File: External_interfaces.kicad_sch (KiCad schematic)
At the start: 31 parts, among them J10 Conn_01x06_Pin, J15 Conn_01x02_Pin, J17 Conn_01x04_Pin, J7 Conn_01x02_Pin, J8 Conn_01x06_Pin, J9 Conn_01x02_Pin, Q1 AO3400A, Q2 AO3400A

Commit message: feat:убрал часть с батарейным питанием, убрал лишние элементы со старого проекта
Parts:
- removed C28, C45, C46, C47, C52: 0.1u, Capacitor_SMD:C_0805_2012Metric_Pad1.18x1.45mm_HandSolder, symbol Device:C_Small
- removed D4, D5: SMAJ30CA, Diode_SMD:D_SMA, symbol Diode:SMAJ30CA
- removed J10, J8: Conn_01x06_Pin, Connector_Hirose:Hirose_DF13-06P-1.25DSA_1x06_P1.25mm_Vertical, symbol Connector:Conn_01x06_Pin
- removed J15, J7: Conn_01x02_Pin, Connector_PinHeader_2.54mm:PinHeader_1x02_P2.54mm_Vertical, symbol Connector:Conn_01x02_Pin
- removed J17: Conn_01x04_Pin, Connector_PinSocket_2.54mm:PinSocket_1x04_P2.54mm_Vertical, symbol Connector:Conn_01x04_Pin
- removed J9: Conn_01x02_Pin, Connector_Hirose:Hirose_DF13-02P-1.25DSA_1x02_P1.25mm_Vertical, symbol Connector:Conn_01x02_Pin
- removed Q1, Q2: AO3400A, Package_TO_SOT_SMD:SOT-23, symbol Transistor_FET:AO3400A
- removed R23, R24, R27, R28, R31, R32: 0, Resistor_SMD:R_0805_2012Metric_Pad1.20x1.40mm_HandSolder, symbol Device:R
- removed R25, R29: 100, Resistor_SMD:R_0805_2012Metric_Pad1.20x1.40mm_HandSolder, symbol Device:R
- removed R26, R30: 10k, Resistor_SMD:R_0805_2012Metric_Pad1.20x1.40mm_HandSolder, symbol Device:R
- removed R7, R8: 3k, Resistor_SMD:R_0805_2012Metric_Pad1.20x1.40mm_HandSolder, symbol Device:R
- removed VD10, VD15, VD2, VD3: GSOT03C-E3-08, Package_TO_SOT_SMD:SOT-23, symbol TWS:GSOT03C-E3-08
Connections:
- no-connect marks 4 -> 0

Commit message: feaat: добавлены светодиоды, кнопки и недостающие элементы защиты питания
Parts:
- added C60, C61, C62, C63, C64, C65, C66, C67, C68, C69, C70, C71: 0.1u, Capacitor_SMD:C_0805_2012Metric_Pad1.18x1.45mm_HandSolder, symbol Device:C_Small
- added R28, R33, R34, R35, R37, R38, R39, R40, R41, R42, R43, R44: 100, Resistor_SMD:R_0805_2012Metric_Pad1.20x1.40mm_HandSolder, symbol Device:R
- added SW1, SW10, SW11, SW12, SW2, SW3, SW4, SW5, SW6, SW7, SW8, SW9: SW_Push, Button_Switch_THT:SW_PUSH_6mm, symbol Switch:SW_Push
- added VD10, VD4, VD5, VD7, VD8, VD9: GSOT03C-E3-08, Package_TO_SOT_SMD:SOT-23_Handsoldering, symbol TVS_1:GSOT03C-E3-08
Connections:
- new net: C71.2, R44.1
- new net: R44.2, SW12.1, VD10.2 (K2)
- new net: R33.2, SW2.1, VD4.2 (K2)
- new net: R37.2, SW5.1, VD7.1 (K1)
- new net: R39.2, SW7.1, VD8.1 (K1)
- new net: R40.2, SW8.1, VD8.2 (K2)
- new net: C70.2, R43.1
- new net: C65.2, R42.1
- new net: R42.2, SW10.1, VD9.2 (K2)
- new net: R41.2, SW9.1, VD9.1 (K1)
- new net: R34.2, SW3.1, VD5.1 (K1)
- new net: R35.2, SW4.1, VD5.2 (K2)
- new net: R43.2, SW11.1, VD10.1 (K1)
- new net: C62.2, R37.1
- new net: C64.2, R41.1
- new net: R28.2, SW1.1, VD4.1 (K1)
- new net: C69.2, R40.1
- new net: C63.2, R38.1
- new net: R38.2, SW6.1, VD7.2 (K2)
- new net: C68.2, R39.1
- new net DI1: C60.2, R28.1
- new net DI2: C61.2, R33.1
- new net DI3: C67.2, R34.1
- new net DI4: C66.2, R35.1
- new net GND: C60.1, C61.1, C62.1, C63.1, C64.1, C65.1, C66.1, C67.1, C68.1, C69.1, C70.1, C71.1, SW1.2, SW10.2, SW11.2, SW12.2, SW2.2, SW3.2, SW4.2, SW5.2, SW6.2, SW7.2, SW8.2, SW9.2, VD10.3 (A), VD4.3 (A), VD5.3 (A), VD7.3 (A), VD8.3 (A), VD9.3 (A)

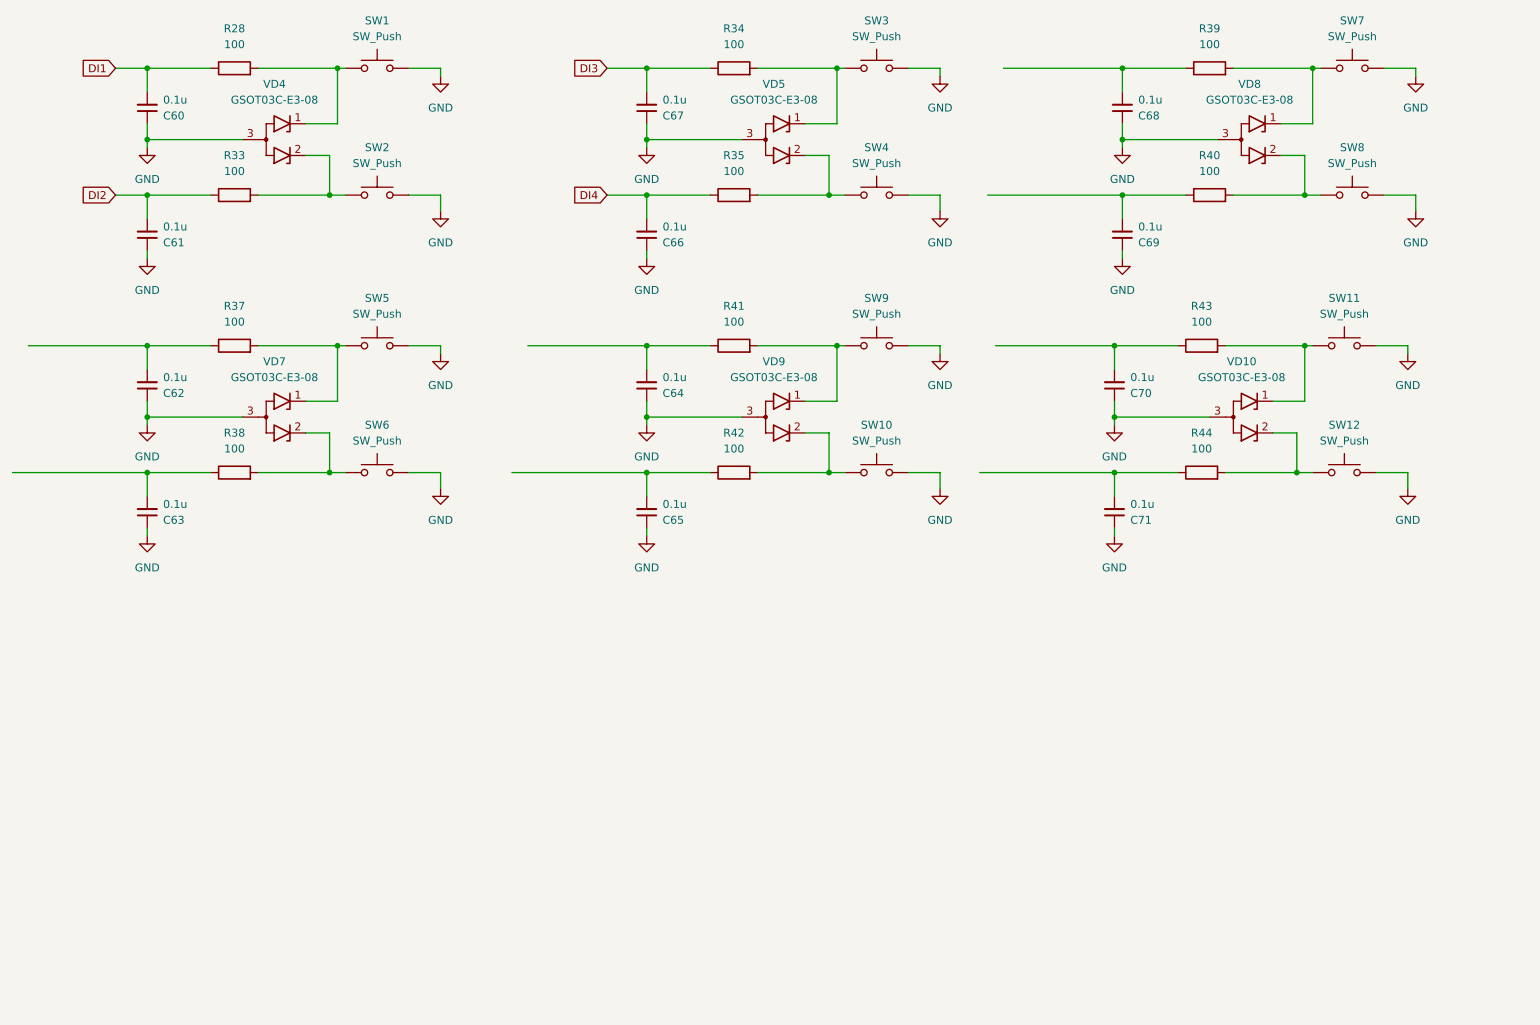
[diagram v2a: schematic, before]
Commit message: feat: добавлены глобальные линии связи, удалены линии связи со старого проекта
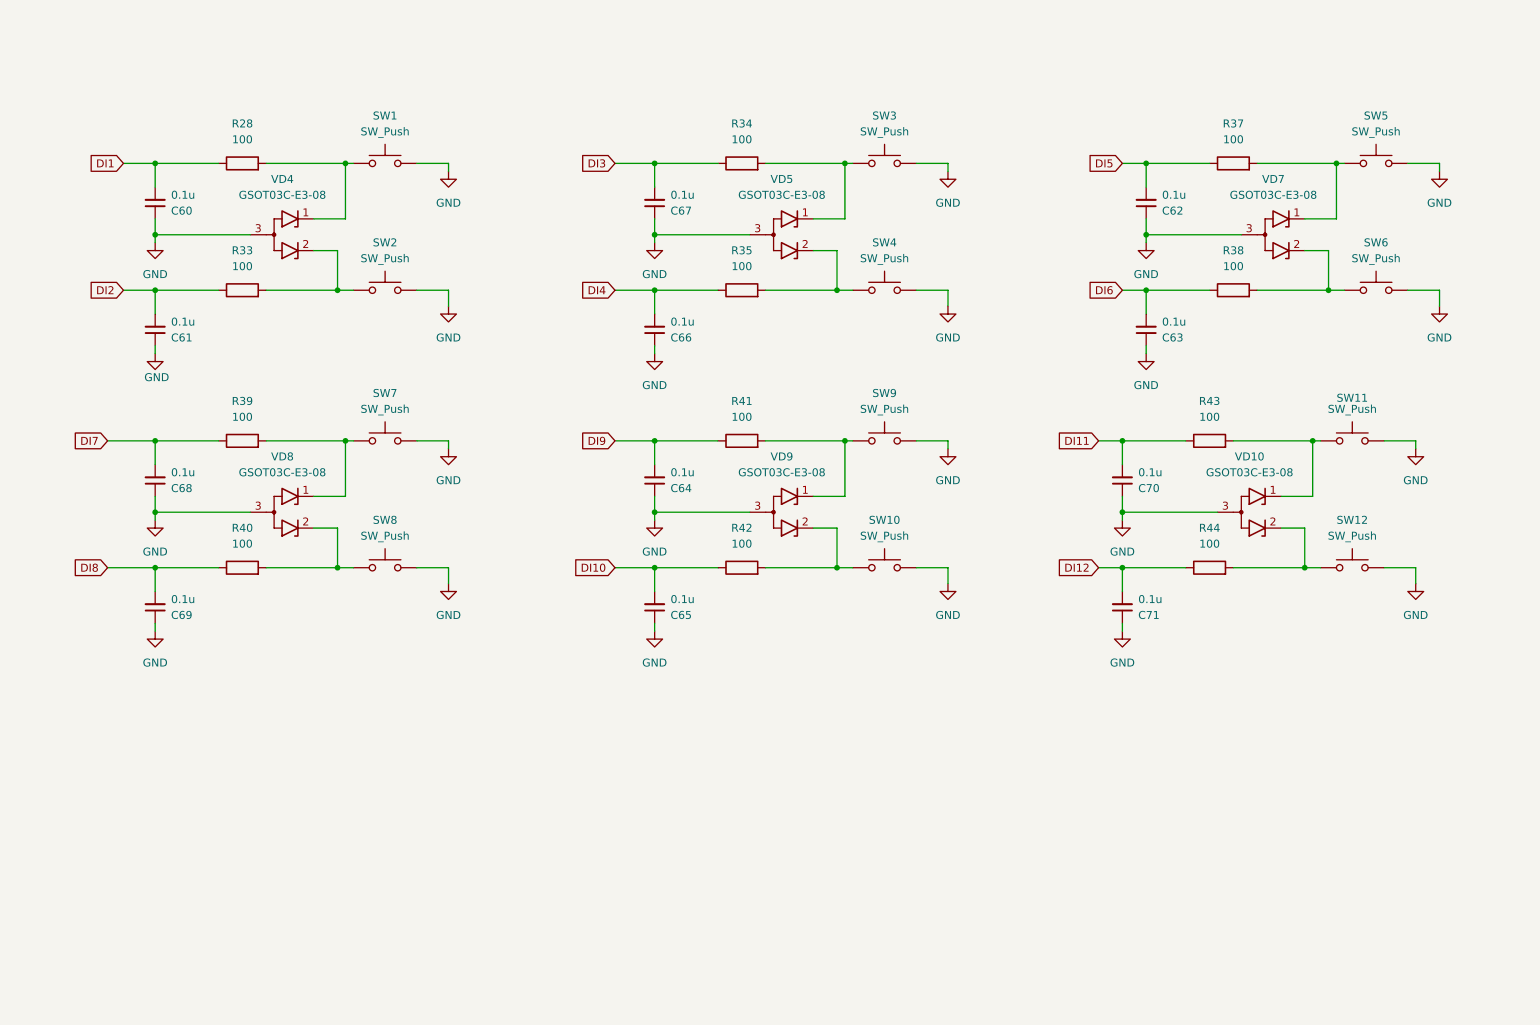
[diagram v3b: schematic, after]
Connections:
- net DI12: now reaches C71.2, R44.1
- net DI11: now reaches C70.2, R43.1
- net DI10: now reaches C65.2, R42.1
- net DI5: now reaches C62.2, R37.1
- net DI9: now reaches C64.2, R41.1
- net DI8: now reaches C69.2, R40.1
- net DI6: now reaches C63.2, R38.1
- net DI7: now reaches C68.2, R39.1
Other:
- moved on the sheet: C60, C61, C62, C63, C64, C65, C66, C67, C68, C69, C70, C71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

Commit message: feat: расположены основные узлы модуля на печатной плате
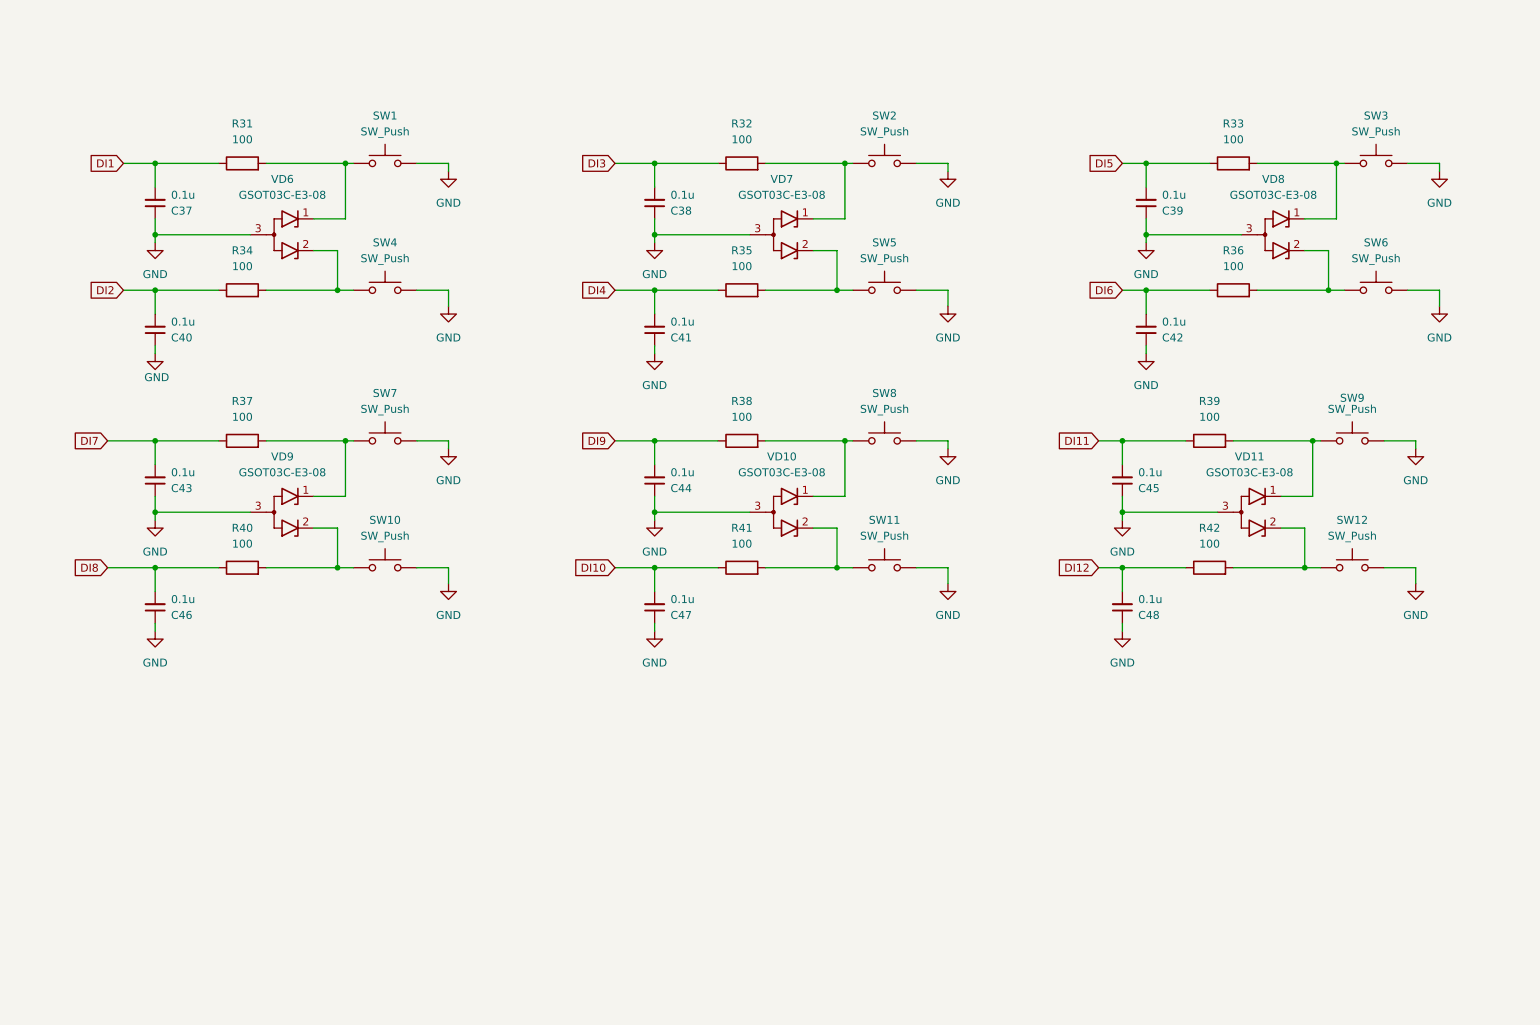
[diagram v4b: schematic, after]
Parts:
- renumbered C60 to C37, C67 to C38, C62 to C39, C61 to C40, C66 to C41, C63 to C42, C68 to C43, C64 to C44, C70 to C45, C69 to C46, C65 to C47, C71 to C48, R28 to R31, R34 to R32, R37 to R33, R33 to R34, R38 to R36, R39 to R37, R41 to R38, R43 to R39, R42 to R41, R44 to R42, SW8 to SW10, SW10 to SW11, SW3 to SW2, SW5 to SW3, SW2 to SW4, SW4 to SW5, SW9 to SW8, SW11 to SW9, VD9 to VD10, VD10 to VD11, VD4 to VD6, VD5 to VD7, VD7 to VD8, VD8 to VD9

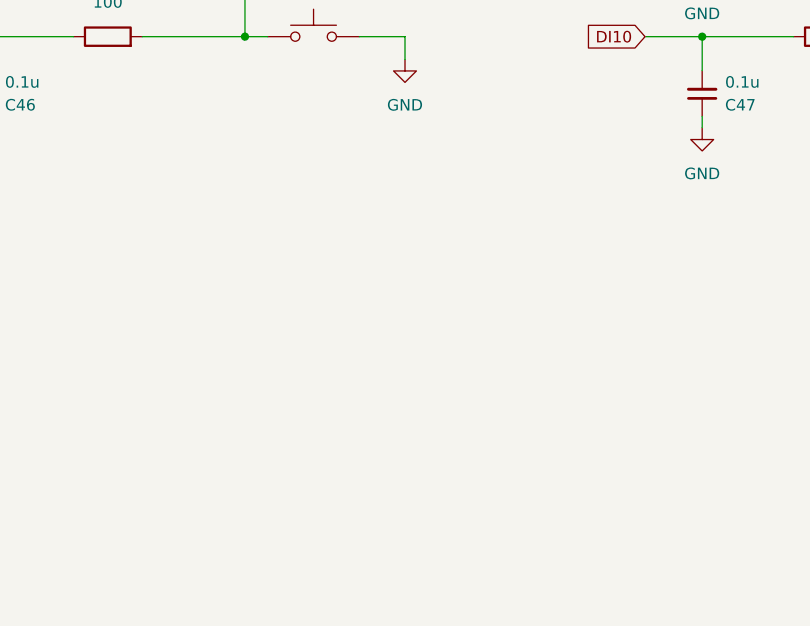
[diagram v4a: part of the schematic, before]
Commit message: feat: добавлена микросхема для коммутации светодиодов
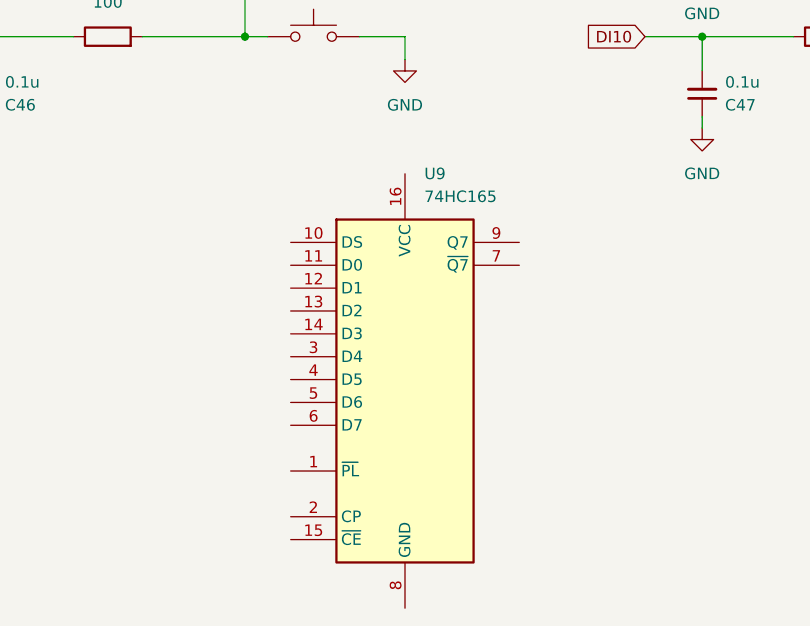
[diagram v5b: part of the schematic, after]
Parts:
- added U9: 74HC165, Package_SO:SOIC-16_3.9x9.9mm_P1.27mm, symbol 74xx:74HC165
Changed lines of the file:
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@@
+	)
+	(symbol
+		(lib_id "74xx:74HC165")
+		(at 97.79 154.94 0)
+		(unit 1)
+		(body_style 1)
+		(exclude_from_sim no)
+		(in_bom yes)
+		(on_board yes)
+		(in_pos_files yes)
+		(dnp no)
+		(fields_autoplaced yes)
+		(property "Reference" "U9"
+			(at 99.9333 132.08 0)
+			(show_name no)
+			(do_not_autoplace no)
+			(effects
+				(font
+					(size 1.27 1.27)
+				)
+				(justify left)
+			)
+		)
+		(property "Value" "74HC165"
+			(at 99.9333 134.62 0)
+			(show_name no)
+			(do_not_autoplace no)
+			(effects
+				(font
+					(size 1.27 1.27)
+				)
+				(justify left)
+			)
+		)
+		(property "Footprint" "Package_SO:SOIC-16_3.9x9.9mm_P1.27mm"
+			(at 97.79 154.94 0)
+			(hide yes)
+			(show_name no)
+			(do_not_autoplace no)
+			(effects
+				(font
+					(size 1.27 1.27)
+				)
+			)
+		)
+		(property "Datasheet" "https://assets.nexperia.com/documents/data-sheet/74HC_HCT165.pdf"
+			(at 97.79 154.94 0)
+			(hide yes)
+			(show_name no)
+			(do_not_autoplace no)
+			(effects
+				(font
+					(size 1.27 1.27)
+				)
+			)
+		)
+		(property "Description" "Shift Register, 8-bit, Parallel Load"
+			(at 97.79 154.94 0)
+			(hide yes)
+			(show_name no)
+			(do_not_autoplace no)
+			(effects
+				(font
+					(size 1.27 1.27)
+				)
+			)
+		)
+		(pin "2"
+		)
+		(pin "7"
+		)
+		(pin "11"
+		)
+		(pin "5"
+		)
+		(pin "1"
+		)
+		(pin "3"
+		)
+		(pin "6"
+		)
+		(pin "4"
+		)
+		(pin "8"
+		)
+		(pin "9"
+		)
+		(pin "10"
+		)
+		(pin "16"
+		)
+		(pin "15"
+		)
+		(pin "13"
+		)
+		(pin "14"
+		)
+		(pin "12"
+		)
+		(instances
+			(project "Magister_work_v1"
+				(path "/9ff4e5e8-ab59-4c4d-a10a-f8f5e444c5cb/15a36b06-8454-4363-8de9-e6e1cabaaceb"
+					(reference "U9")
+					(unit 1)
+				)
+			)
+		)
 	)
 	(symbol

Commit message: feat: добавлены соединения светодиодов и защитных диодов и кнопок
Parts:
- VD10, VD11, VD6, VD7, VD8, VD9: footprint Package_TO_SOT_SMD:SOT-23_Handsoldering -> Package_TO_SOT_SMD:SOT-23
- renumbered SW11 to SW10, SW9 to SW11, SW4 to SW2, SW2 to SW3, SW5 to SW4, SW3 to SW5, SW10 to SW8, SW8 to SW9
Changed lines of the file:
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@@
 		(dnp no)
 		(fields_autoplaced yes)
-		(property "Reference" "SW4"
+		(property "Reference" "SW2"
 			(at 87.63 64.77 0)
 			(show_name no)
@@
 			(project "Magister_work_v1"
 				(path "/9ff4e5e8-ab59-4c4d-a10a-f8f5e444c5cb/15a36b06-8454-4363-8de9-e6e1cabaaceb"
-					(reference "SW4")
+					(reference "SW2")
 					(unit 1)
 				)
@@
 		(dnp no)
 		(fields_autoplaced yes)
-		(property "Reference" "SW3"
+		(property "Reference" "SW5"
 			(at 246.38 44.45 0)
 			(show_name no)
@@
 			(project "Magister_work_v1"
 				(path "/9ff4e5e8-ab59-4c4d-a10a-f8f5e444c5cb/15a36b06-8454-4363-8de9-e6e1cabaaceb"
-					(reference "SW3")
+					(reference "SW5")
 					(unit 1)
 				)
@@
 			)
 		)
-		(property "Footprint" "Package_TO_SOT_SMD:SOT-23_Handsoldering"
+		(property "Footprint" "Package_TO_SOT_SMD:SOT-23"
 			(at 71.12 115.57 0)
 			(hide yes)
@@
 		(dnp no)
 		(fields_autoplaced yes)
-		(property "Reference" "SW8"
+		(property "Reference" "SW9"
 			(at 167.64 88.9 0)
 			(show_name no)
@@
 			(project "Magister_work_v1"
 				(path "/9ff4e5e8-ab59-4c4d-a10a-f8f5e444c5cb/15a36b06-8454-4363-8de9-e6e1cabaaceb"
-					(reference "SW8")
+					(reference "SW9")
 					(unit 1)
 				)
@@
 			)
 		)
-		(property "Footprint" "Package_TO_SOT_SMD:SOT-23_Handsoldering"
+		(property "Footprint" "Package_TO_SOT_SMD:SOT-23"
 			(at 151.13 71.12 0)
 			(hide yes)
@@
 			)
 		)
-		(property "Footprint" "Package_TO_SOT_SMD:SOT-23_Handsoldering"
+		(property "Footprint" "Package_TO_SOT_SMD:SOT-23"
 			(at 226.06 115.57 0)
 			(hide yes)
@@
 		(dnp no)
 		(fields_autoplaced yes)
-		(property "Reference" "SW10"
+		(property "Reference" "SW8"
 			(at 87.63 109.22 0)
 			(show_name no)
@@
 			(project "Magister_work_v1"
 				(path "/9ff4e5e8-ab59-4c4d-a10a-f8f5e444c5cb/15a36b06-8454-4363-8de9-e6e1cabaaceb"
-					(reference "SW10")
+					(reference "SW8")
 					(unit 1)
 				)
@@
 		(in_pos_files yes)
 		(dnp no)
-		(property "Reference" "SW9"
+		(property "Reference" "SW11"
 			(at 242.57 89.662 0)
 			(show_name no)
@@
 			(project "Magister_work_v1"
 				(path "/9ff4e5e8-ab59-4c4d-a10a-f8f5e444c5cb/15a36b06-8454-4363-8de9-e6e1cabaaceb"
-					(reference "SW9")
+					(reference "SW11")
 					(unit 1)
 				)
@@
 			)
 		)
-		(property "Footprint" "Package_TO_SOT_SMD:SOT-23_Handsoldering"
+		(property "Footprint" "Package_TO_SOT_SMD:SOT-23"
 			(at 151.13 115.57 0)
 			(hide yes)
@@
 		(dnp no)
 		(fields_autoplaced yes)
-		(property "Reference" "SW2"
+		(property "Reference" "SW3"
 			(at 167.64 44.45 0)
 			(show_name no)
@@
 			(project "Magister_work_v1"
 				(path "/9ff4e5e8-ab59-4c4d-a10a-f8f5e444c5cb/15a36b06-8454-4363-8de9-e6e1cabaaceb"
-					(reference "SW2")
+					(reference "SW3")
 					(unit 1)
 				)
@@
 			)
 		)
-		(property "Footprint" "Package_TO_SOT_SMD:SOT-23_Handsoldering"
+		(property "Footprint" "Package_TO_SOT_SMD:SOT-23"
 			(at 71.12 71.12 0)
 			(hide yes)
@@
 			)
 		)
-		(property "Footprint" "Package_TO_SOT_SMD:SOT-23_Handsoldering"
+		(property "Footprint" "Package_TO_SOT_SMD:SOT-23"
 			(at 229.87 71.12 0)
 			(hide yes)
@@
 		(dnp no)
 		(fields_autoplaced yes)
-		(property "Reference" "SW5"
+		(property "Reference" "SW4"
 			(at 167.64 64.77 0)
 			(show_name no)
@@
 			(project "Magister_work_v1"
 				(path "/9ff4e5e8-ab59-4c4d-a10a-f8f5e444c5cb/15a36b06-8454-4363-8de9-e6e1cabaaceb"
-					(reference "SW5")
+					(reference "SW4")
 					(unit 1)
 				)
@@
 		(dnp no)
 		(fields_autoplaced yes)
-		(property "Reference" "SW11"
+		(property "Reference" "SW10"
 			(at 167.64 109.22 0)
 			(show_name no)
@@
 			(project "Magister_work_v1"
 				(path "/9ff4e5e8-ab59-4c4d-a10a-f8f5e444c5cb/15a36b06-8454-4363-8de9-e6e1cabaaceb"
-					(reference "SW11")
+					(reference "SW10")
 					(unit 1)
 				)

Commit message: feat: разведена обвыязка кнопок
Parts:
- removed U9: 74HC165, Package_SO:SOIC-16_3.9x9.9mm_P1.27mm, symbol 74xx:74HC165
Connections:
- net DI6: now also C43.2, R37.1; no longer C42.2, R36.1
- net DI7: now also C42.2, R36.1; no longer C43.2, R37.1
- net GND: no longer VD9.3 (A)
- net at R37.2, SW7.1: now also VD8.2 (K2); no longer VD9.1 (K1)
- net at R36.2, SW6.1: now also VD9.1 (K1); no longer VD8.2 (K2)
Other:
- moved on the sheet: C42, C43, R36, R37, SW6, SW7
